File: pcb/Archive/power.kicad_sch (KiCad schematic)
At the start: 21 parts, among them U5 LM66200DRLR, U6 LM66200DRLR, U7 LD1117S33TR

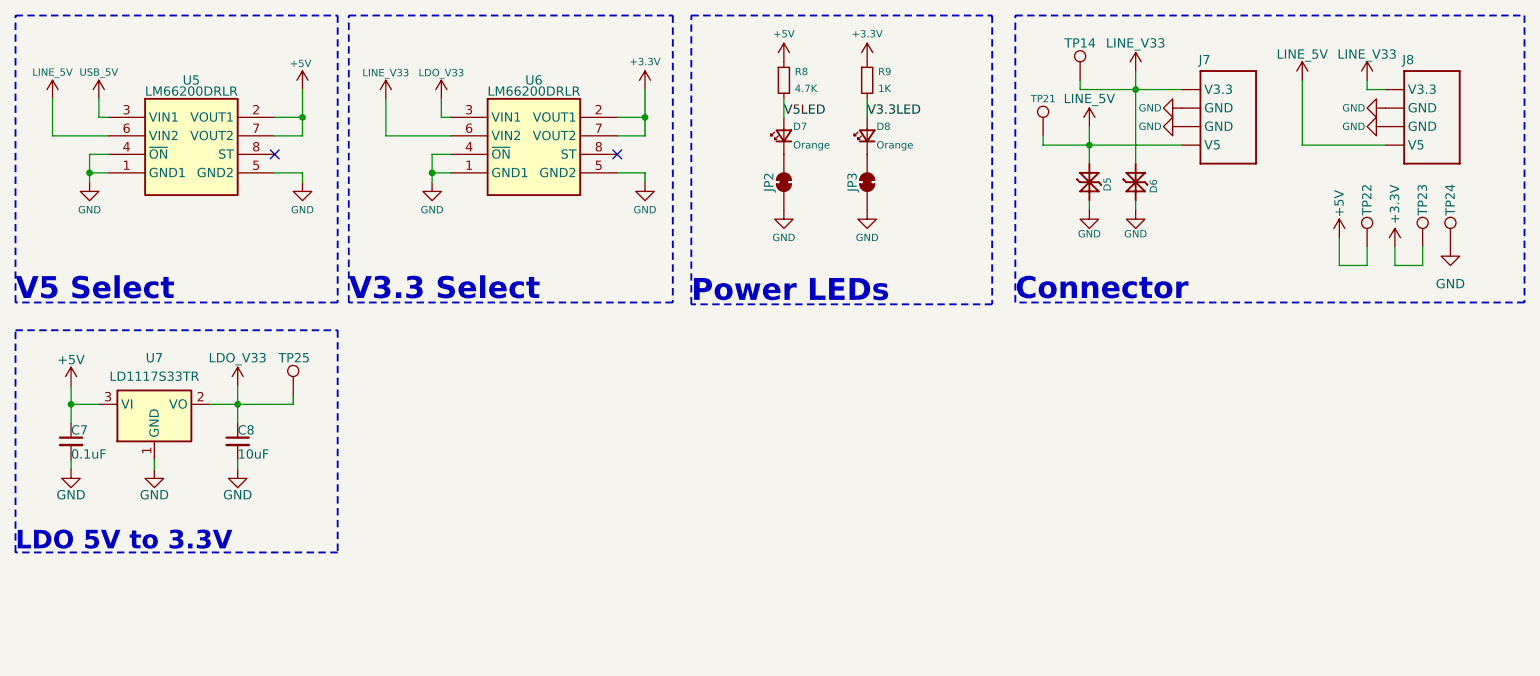
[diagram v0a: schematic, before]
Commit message: Added interfaces and fully routed PCB
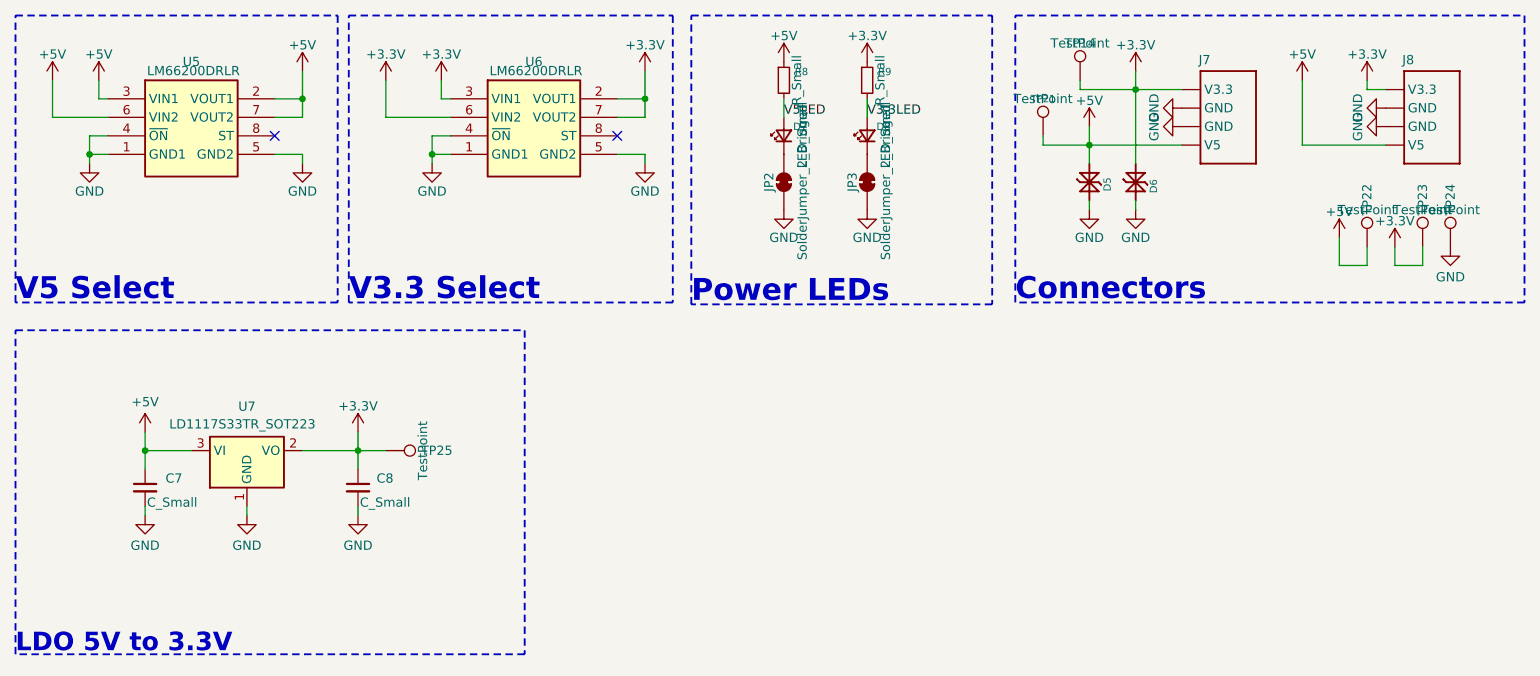
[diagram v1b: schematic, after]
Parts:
- C7: value 0.1uF -> C_Small; footprint Capacitor_SMD:C_0603_1608Metric -> (none); Digikey 1276-1005-2-ND -> (none); LCSC C66501 -> (none); MF Samsung -> (none); MPN CL10B104KO8NNNC -> (none); Mouser 187-CL10B104KO8NNNC -> (none)
- C8: value 10uF -> C_Small; footprint Capacitor_SMD:C_0603_1608Metric -> (none); Digikey 1276-1870-2-ND -> (none); LCSC C92487 -> (none); MF Samsung -> (none); MPN CL10A106MO8NQNC -> (none); Mouser 187-CL10A106MO8NQNC -> (none)
- D6: MN FUXINSEMI -> (none); MPN LESD8D3.3CAT5G -> (none)
- D7, D8: value Orange -> LED_Small; footprint LED_SMD:LED_0603_1608Metric -> (none); Digikey 5962-XL-1608UOC-06TR-ND -> (none); LCSC C965800 -> (none); MN XINGLIGHT -> (none); MPN XL-1608UOC-06 -> (none); Mouser 859-LTST-C190KFKT -> (none)
- J7, J8: value ~ -> (none); footprint CRGM Connector:JST_SH_SM04B-SRSS-TB_1x04-1MP_P1.00mm_Horizontal -> CRGM Connector:SM04B-SRSS-TB
- JP2, JP3: value ~ -> SolderJumper_2_Bridged; footprint CRGM Connector:SolderJumper-2_P1.3mm_Bridged_RoundedPad1.0x1.5mm -> (none)
- R8: value 4.7K -> R_Small; footprint Resistor_SMD:R_0603_1608Metric -> (none); Digikey 541-3993-2-ND -> (none); LCSC C2907166 -> (none); MN FOJAN -> (none); MPN FRC0603J472 TS -> (none); Mouser 71-CRCW06034K70JNEAC -> (none)
- R9: value 1K -> R_Small; footprint Resistor_SMD:R_0603_1608Metric -> (none); Digikey 541-3991-2-ND -> (none); LCSC C2907113 -> (none); MN Vishay -> (none); MPN CRCW06031K00FKEA -> (none); Mouser 71-CRCW06031K00JNEAC -> (none)
- TP14, TP21, TP22, TP23, TP24, TP25: value ~ -> TestPoint; footprint CRGM Mechanical:TestPoint_Pad_D1.0mm -> (none); now in the parts list
- U7: value LD1117S33TR -> LD1117S33TR_SOT223; footprint CRGM Power:SOT230P700X180-4N -> Package_TO_SOT_SMD:SOT-223-3_TabPin2; Digikey 497-1242-2-ND -> (none); LCSC_PN C86781 -> (none); MF STMicroeletronics -> (none); MPN LD1117S33TR -> (none); Mouser 511-LD1117S33 -> (none)
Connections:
- net LDO_V33 is gone; now on net +3.3V: C8.1, TP25.1, U6.3 (VIN1), U7.2 (VO)
- net LINE_5V is gone; now on net +5V: D5.2 (K2), J7.1 (V5), J8.1 (V5), TP21.1, U5.6 (VIN2)
- net LINE_V33 is gone; now on net +3.3V: D6.2 (K2), J7.4 (V3.3), J8.4 (V3.3), TP14.1, U6.6 (VIN2)
- net USB_5V is gone; now on net +5V: U5.3 (VIN1)
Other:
- note added: "Connectors"
- note removed: "Connector"
- moved on the sheet: C7, C8, TP25, U5, U6, U7
